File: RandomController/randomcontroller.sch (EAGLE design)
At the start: 103 parts, among them IC1 TPS2054B, IC2 TPS2054B, IC3 TPS2054B, IC4 TPS2054B, IC6 PIC16F1939PT, Q1 NX-3215, U1 MCP1700_SOT23

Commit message: random controller first version
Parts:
- removed R10, R11, R12, R13, R14, R15, R16, R17, R18, R19, R20, R21, R22, R8, R9: 10k, WaterDrop:R0805(2012)
- added C15: 0.1uF, WaterDrop:C0805(2012)
- added C16: (no value), yBrainDigital:C-TANTAL-A
- added H1, H2, H3, H4: MOUNT-PAD-ROUND3.2, holes:MOUNT-PAD-ROUND3.2
- added LED17: (no value), adafruit:LEDCHIPLED_0805
- added U$1: LOGO, WaterDrop:LOGO
- R7: value 10k -> 2.2k
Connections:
- removed net N$33: IC1.P$13, R8.1
- removed net N$34: IC1.P$12, R9.1
- removed net N$35: IC1.P$9, R10.1
- removed net N$36: IC2.P$16, R11.1
- removed net N$37: IC2.P$13, R12.1
- removed net N$38: IC2.P$12, R13.1
- removed net N$39: IC2.P$9, R14.1
- removed net N$40: IC3.P$16, R15.1
- removed net N$41: IC3.P$13, R16.1
- removed net N$42: IC3.P$12, R17.1
- removed net N$43: IC3.P$9, R18.1
- removed net N$44: IC4.P$16, R19.1
- removed net N$45: IC4.P$13, R20.1
- removed net N$46: IC4.P$12, R21.1
- removed net N$47: IC4.P$9, R22.1
- net +3.3V: no longer R10.2, R11.2, R12.2, R13.2, R14.2, R15.2, R16.2, R17.2, R18.2, R19.2, R20.2, R21.2, R22.2, R7.2, R8.2, R9.2
- net +5V: now also C15.1, C16.+
- net CLKOUT: now also R7.2
- net GND: now also C15.2, C16.-, LED17.C
- net N$3: no longer D2.P$1
- net N$32: now also LED17.A; no longer IC1.P$16
- net N$4: now also D2.P$1
- net STRUT_GND: now also H1.MOUNT, H2.MOUNT
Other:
- note added: "1"
- note added: "16"
- moved on the sheet: D2, R3, R7

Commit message: waterdrop and random controller gerber
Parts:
- R1: value 1M -> 620k
- R2, R23, R24, R25, R26, R27, R28, R29, R30, R31, R32, R33, R34, R35, R36, R37, R7: value 2.2k -> 1k
- R38: value 10k -> 100k
- R4: value (none) -> 1k
- RN1, RN2: value (none) -> 4.7k

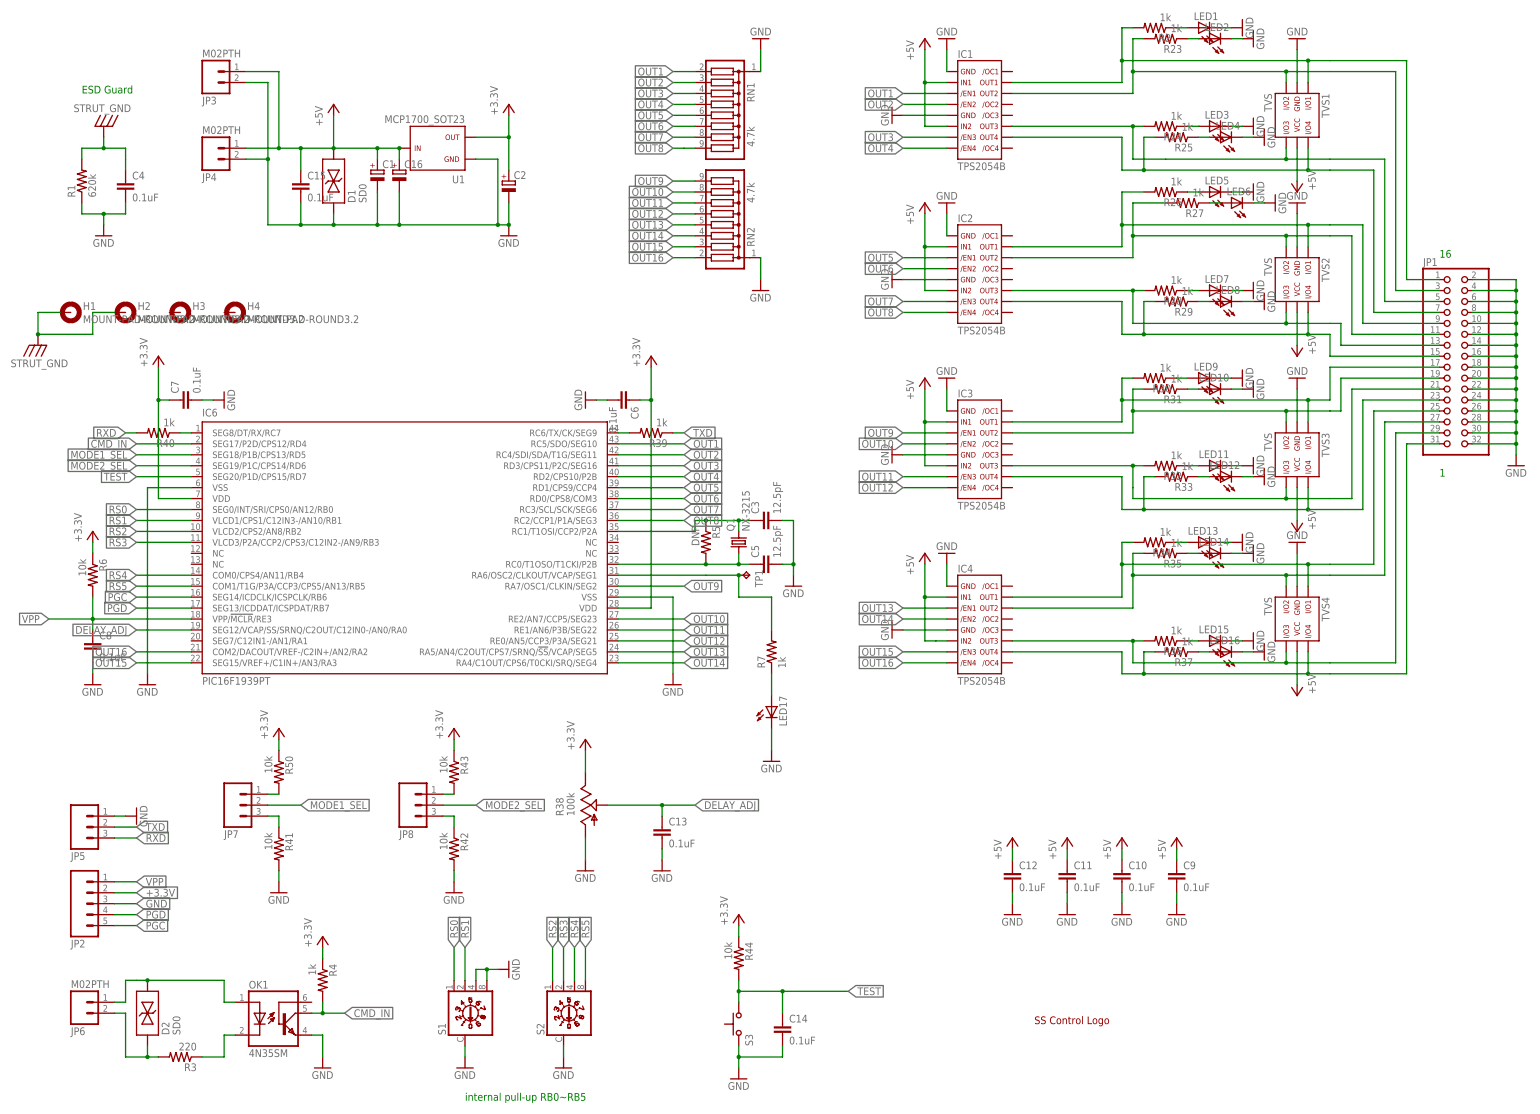
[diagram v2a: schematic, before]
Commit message: schmatic renumbered final merged gerber for fab
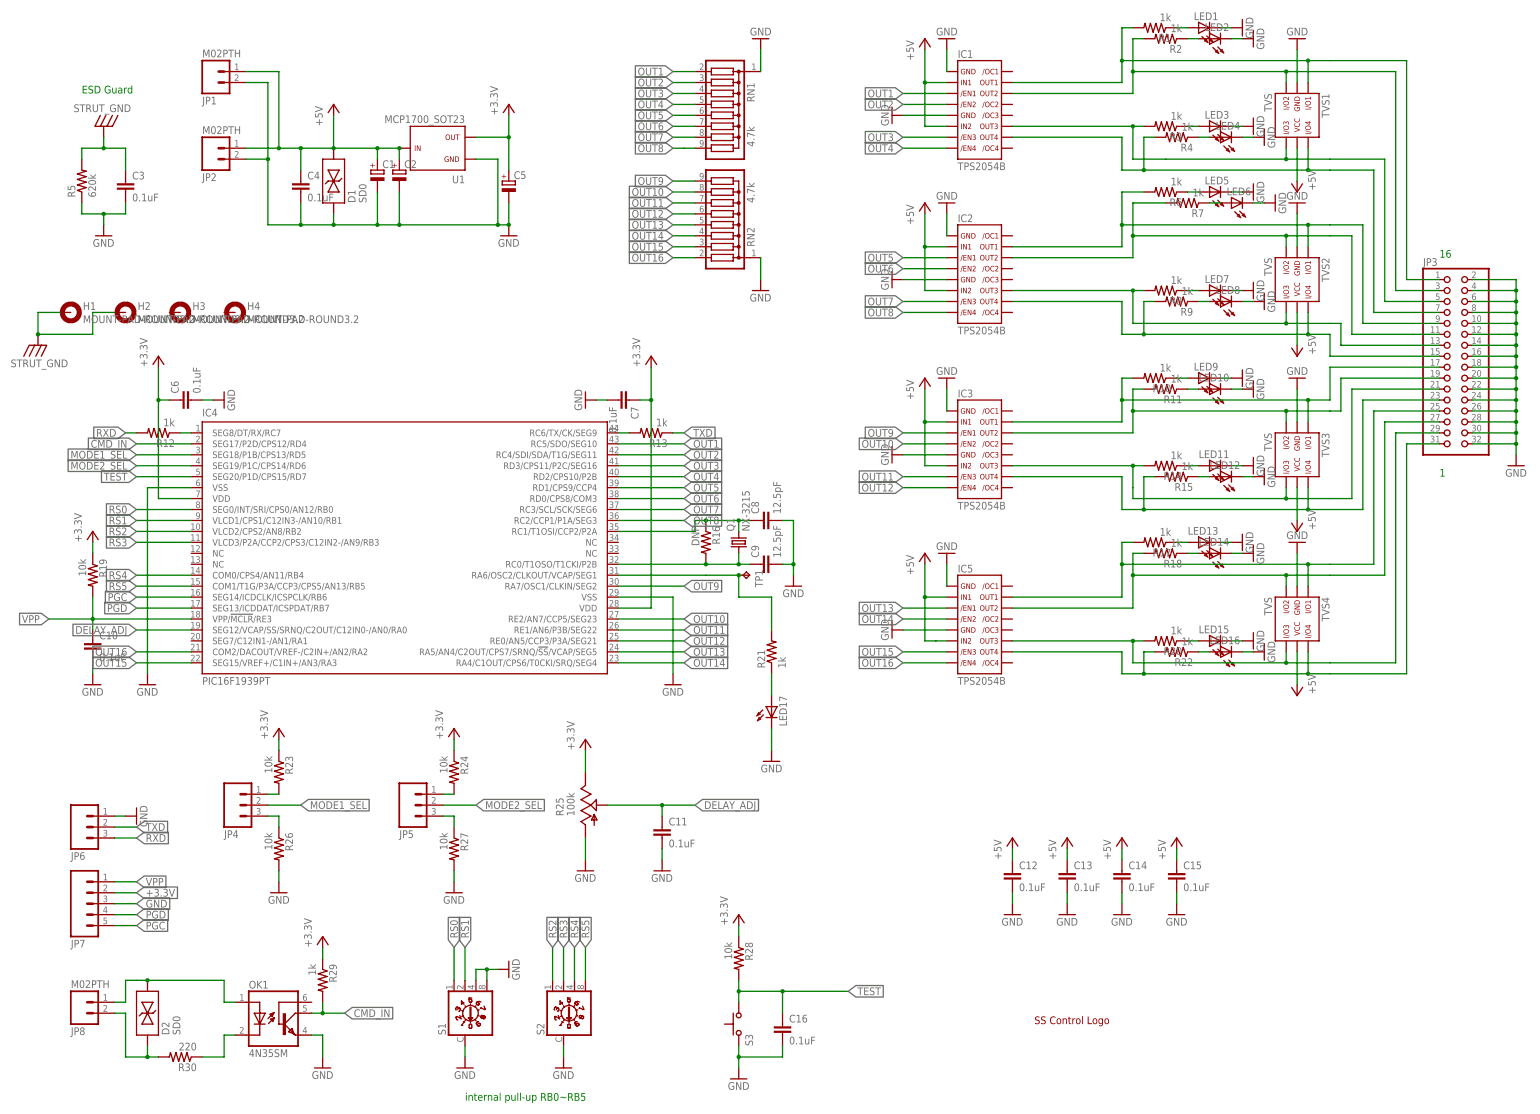
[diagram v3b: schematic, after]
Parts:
- removed IC6: PIC16F1939PT, microchip:PIC16F1939PT
- removed R38: 100k, pot:TRIM_US-B25P
- removed R41, R42, R43, R44, R50: 10k, WaterDrop:R0805(2012)
- added IC5: TPS2054B, WaterDrop:TPS2054B
- added R10, R21, R8, R9: 1k, WaterDrop:R0805(2012)
- added R16: DNP, WaterDrop:R0805(2012)
- added R19: 10k, WaterDrop:R0805(2012)
- C16: value (none) -> 0.1uF; device yBrainDigital:C-TANTAL-A -> WaterDrop:C0805(2012)
- C3: value 12.5pF -> 0.1uF
- C5: value 12.5pF -> (none); device WaterDrop:C0805(2012) -> yBrainDigital:C-TANTAL-A
- C8, C9: value 0.1uF -> 12.5pF
- IC4: value TPS2054B -> PIC16F1939PT; device WaterDrop:TPS2054B -> microchip:PIC16F1939PT
- JP1: value (none) -> M02PTH; device pinhead:PINHD-2X16/90 -> SparkFun-Connectors:M02PTH
- JP2: value (none) -> M02PTH; device SparkFun-Connectors:M05PTH -> SparkFun-Connectors:M02PTH
- JP3: value M02PTH -> (none); device SparkFun-Connectors:M02PTH -> pinhead:PINHD-2X16/90
- JP4, JP6: value M02PTH -> (none); device SparkFun-Connectors:M02PTH -> SparkFun-Connectors:M03PTH
- JP7: device SparkFun-Connectors:M03PTH -> SparkFun-Connectors:M05PTH
- JP8: value (none) -> M02PTH; device SparkFun-Connectors:M03PTH -> SparkFun-Connectors:M02PTH
- R1: value 620k -> 1k
- R23, R24, R26, R27, R28: value 1k -> 10k
- R25: value 1k -> 100k; device WaterDrop:R0805(2012) -> pot:TRIM_US-B25P
- R3: value 220 -> 1k
- R30: value 1k -> 220
- R5: value DNP -> 620k
- R6: value 10k -> 1k
- renumbered R31 to R11, R32 to R14, R33 to R15, R34 to R17, R35 to R18, R36 to R20, R37 to R22, R39 to R13, R40 to R12
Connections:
- net +3.3V: now also C5.+, IC4.VDD, IC4.VDD@1, JP7.2, R19.1, R23.1, R24.1, R25.E, R28.1, R29.1; no longer C2.+, IC6.VDD, IC6.VDD@1, JP2.2, R38.E, R4.1, R43.1, R44.1, R50.1, R6.1
- net +5V: now also C13.1, C14.1, C2.+, C4.1, IC5.P$2, IC5.P$6, JP1.1, JP2.1; no longer C10.1, C11.1, C16.+, C9.1, IC4.P$2, IC4.P$6, JP3.1, JP4.1
- net CLKOUT: now also IC4.RA6/OSC2/CLKOUT/VCAP/SEG1, R21.2; no longer IC6.RA6/OSC2/CLKOUT/VCAP/SEG1, R7.2
- net CMD_IN: now also IC4.SEG17/P2D/CPS12/RD4, R29.2; no longer IC6.SEG17/P2D/CPS12/RD4, R4.2
- net DELAY_ADJ: now also C11.1, IC4.SEG12/VCAP/SS/SRNQ/C2OUT/C12IN0-/AN0/RA0, R25.S; no longer C13.1, IC6.SEG12/VCAP/SS/SRNQ/C2OUT/C12IN0-/AN0/RA0, R38.S
- net GND: now also C16.2, C5.-, IC4.VSS, IC4.VSS@1, IC5.P$1, IC5.P$5, JP2.2, JP3.10, JP3.12, JP3.14, JP3.16, JP3.18, JP3.20, JP3.22, JP3.24, JP3.26, JP3.28, JP3.30, JP3.32, JP3.4, JP3.6, JP3.8, JP6.1, JP7.3, R25.A, R26.2, R27.2, R5.1; no longer C16.-, C5.2, IC4.P$1, IC4.P$5, IC6.VSS, IC6.VSS@1, JP1.10, JP1.12, JP1.14, JP1.16, JP1.18, JP1.20, JP1.22, JP1.24, JP1.26, JP1.28, JP1.30, JP1.32, JP1.4, JP1.6, JP1.8, JP2.3, JP4.2, JP5.1, R1.1, R38.A, R41.2, R42.2
- net MODE1_SEL: now also IC4.SEG18/P1B/CPS13/RD5, JP4.2; no longer IC6.SEG18/P1B/CPS13/RD5, JP7.2
- net MODE2_SEL: now also IC4.SEG19/P1C/CPS14/RD6, JP5.2; no longer IC6.SEG19/P1C/CPS14/RD6, JP8.2
- net N$1: now also JP8.1; no longer JP6.1
- net N$10: now also R6.1; no longer R26.1
- net N$11: now also R7.1; no longer R27.1
- net N$12: now also JP3.1, R1.2; no longer JP1.1, R2.2
- net N$13: now also JP3.3, R2.2; no longer JP1.3, R23.2
- net N$14: now also JP3.5, R3.2; no longer JP1.5, R24.2
- net N$15: now also JP3.7, R4.2; no longer JP1.7, R25.2
- net N$16: now also JP3.9, R6.2; no longer JP1.9, R26.2
- net N$17: now also JP3.11, R7.2; no longer JP1.11, R27.2
- net N$18: now also JP3.13, R8.2; no longer JP1.13, R28.2
- net N$19: now also JP3.15, R9.2; no longer JP1.15, R29.2
- net N$2: now also R1.1; no longer R2.1
- net N$20: now also JP3.19; no longer JP1.19
- net N$21: now also JP3.21; no longer JP1.21
- net N$22: now also JP3.23; no longer JP1.23
- net N$23: now also JP3.17, R10.2; no longer JP1.17, R30.2
- net N$24: now also IC5.P$14, JP3.27; no longer IC4.P$14, JP1.27
- net N$25: now also IC5.P$15, JP3.25; no longer IC4.P$15, JP1.25
- net N$26: now also IC5.P$11, JP3.29; no longer IC4.P$11, JP1.29
- net N$27: now also IC5.P$10, JP3.31; no longer IC4.P$10, JP1.31
- net N$28: now also R10.1; no longer R30.1
- net N$3: now also R30.1; no longer R3.1
- net N$32: now also R21.1; no longer R7.1
- net N$4: now also JP8.2, R30.2; no longer JP6.2, R3.2
- net N$5: now also R2.1; no longer R23.1
- net N$52: now also R8.1; no longer R28.1
- net N$53: now also R9.1; no longer R29.1
- net N$54: now also IC4.SEG8/DT/RX/RC7; no longer IC6.SEG8/DT/RX/RC7
- net N$55: now also IC4.RC6/TX/CK/SEG9; no longer IC6.RC6/TX/CK/SEG9
- net N$56: now also JP5.1, R24.2; no longer JP8.1, R43.2
- net N$57: now also JP4.1, R23.2; no longer JP7.1, R50.2
- net N$58: now also JP4.3, R26.1; no longer JP7.3, R41.1
- net N$59: now also JP5.3, R27.1; no longer JP8.3, R42.1
- net N$6: now also C8.1, IC4.RC1/T1OSI/CCP2/P2A, R16.1; no longer C3.1, IC6.RC1/T1OSI/CCP2/P2A, R5.1
- net N$7: now also C9.1, IC4.RC0/T1OSO/T1CKI/P2B, R16.2; no longer C5.1, IC6.RC0/T1OSO/T1CKI/P2B, R5.2
- net N$8: now also R3.1; no longer R24.1
- net N$9: now also R4.1; no longer R25.1
- net OUT1: now also IC4.RC5/SDO/SEG10; no longer IC6.RC5/SDO/SEG10
- net OUT10: now also IC4.RE2/AN7/CCP5/SEG23; no longer IC6.RE2/AN7/CCP5/SEG23
- net OUT11: now also IC4.RE1/AN6/P3B/SEG22; no longer IC6.RE1/AN6/P3B/SEG22
- net OUT12: now also IC4.RE0/AN5/CCP3/P3A/SEG21; no longer IC6.RE0/AN5/CCP3/P3A/SEG21
- net OUT13: now also IC4.RA5/AN4/C2OUT/CPS7/SRNQ/!SS!/VCAP/SEG5, IC5.P$3; no longer IC4.P$3, IC6.RA5/AN4/C2OUT/CPS7/SRNQ/!SS!/VCAP/SEG5
- net OUT14: now also IC4.RA4/C1OUT/CPS6/T0CKI/SRQ/SEG4, IC5.P$4; no longer IC4.P$4, IC6.RA4/C1OUT/CPS6/T0CKI/SRQ/SEG4
- net OUT15: now also IC4.SEG15/VREF+/C1IN+/AN3/RA3, IC5.P$7; no longer IC4.P$7, IC6.SEG15/VREF+/C1IN+/AN3/RA3
- net OUT16: now also IC4.COM2/DACOUT/VREF-/C2IN+/AN2/RA2, IC5.P$8; no longer IC4.P$8, IC6.COM2/DACOUT/VREF-/C2IN+/AN2/RA2
- net OUT2: now also IC4.RC4/SDI/SDA/T1G/SEG11; no longer IC6.RC4/SDI/SDA/T1G/SEG11
- net OUT3: now also IC4.RD3/CPS11/P2C/SEG16; no longer IC6.RD3/CPS11/P2C/SEG16
- net OUT4: now also IC4.RD2/CPS10/P2B; no longer IC6.RD2/CPS10/P2B
- net OUT5: now also IC4.RD1/CPS9/CCP4; no longer IC6.RD1/CPS9/CCP4
- net OUT6: now also IC4.RD0/CPS8/COM3; no longer IC6.RD0/CPS8/COM3
- net OUT7: now also IC4.RC3/SCL/SCK/SEG6; no longer IC6.RC3/SCL/SCK/SEG6
- net OUT8: now also IC4.RC2/CCP1/P1A/SEG3; no longer IC6.RC2/CCP1/P1A/SEG3
- net OUT9: now also IC4.RA7/OSC1/CLKIN/SEG2; no longer IC6.RA7/OSC1/CLKIN/SEG2
- net PGC: now also IC4.SEG14/ICDCLK/ICSPCLK/RB6, JP7.5; no longer IC6.SEG14/ICDCLK/ICSPCLK/RB6, JP2.5
- net PGD: now also IC4.SEG13/ICDDAT/ICSPDAT/RB7, JP7.4; no longer IC6.SEG13/ICDDAT/ICSPDAT/RB7, JP2.4
- net RS0: now also IC4.SEG0/INT/SRI/CPS0/AN12/RB0; no longer IC6.SEG0/INT/SRI/CPS0/AN12/RB0
- net RS1: now also IC4.VLCD1/CPS1/C12IN3-/AN10/RB1; no longer IC6.VLCD1/CPS1/C12IN3-/AN10/RB1
- net RS2: now also IC4.VLCD2/CPS2/AN8/RB2; no longer IC6.VLCD2/CPS2/AN8/RB2
- net RS3: now also IC4.VLCD3/P2A/CCP2/CPS3/C12IN2-/AN9/RB3; no longer IC6.VLCD3/P2A/CCP2/CPS3/C12IN2-/AN9/RB3
- net RS4: now also IC4.COM0/CPS4/AN11/RB4; no longer IC6.COM0/CPS4/AN11/RB4
- net RS5: now also IC4.COM1/T1G/P3A/CCP3/CPS5/AN13/RB5; no longer IC6.COM1/T1G/P3A/CCP3/CPS5/AN13/RB5
- net RXD: now also JP6.3; no longer JP5.3
- net STRUT_GND: now also C3.1, R5.2; no longer C4.1, R1.2
- net TEST: now also C16.1, IC4.SEG20/P1D/CPS15/RD7, R28.2; no longer C14.1, IC6.SEG20/P1D/CPS15/RD7, R44.2
- net TXD: now also JP6.2; no longer JP5.2
- net VPP: now also C10.1, IC4.VPP/!MCLR!/RE3, JP7.1, R19.2; no longer C8.1, IC6.VPP/!MCLR!/RE3, JP2.1, R6.2
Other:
- moved on the sheet: C10, C11, C13, C14, C15, C2, C3, C4, C6, C7, C8, C9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
